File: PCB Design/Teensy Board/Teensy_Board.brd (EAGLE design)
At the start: 100 x 80 mm, 8 parts, among them IC1 MC7805BDTRKG, IC2 UA78M33CKVU, X1 RJ45-8X

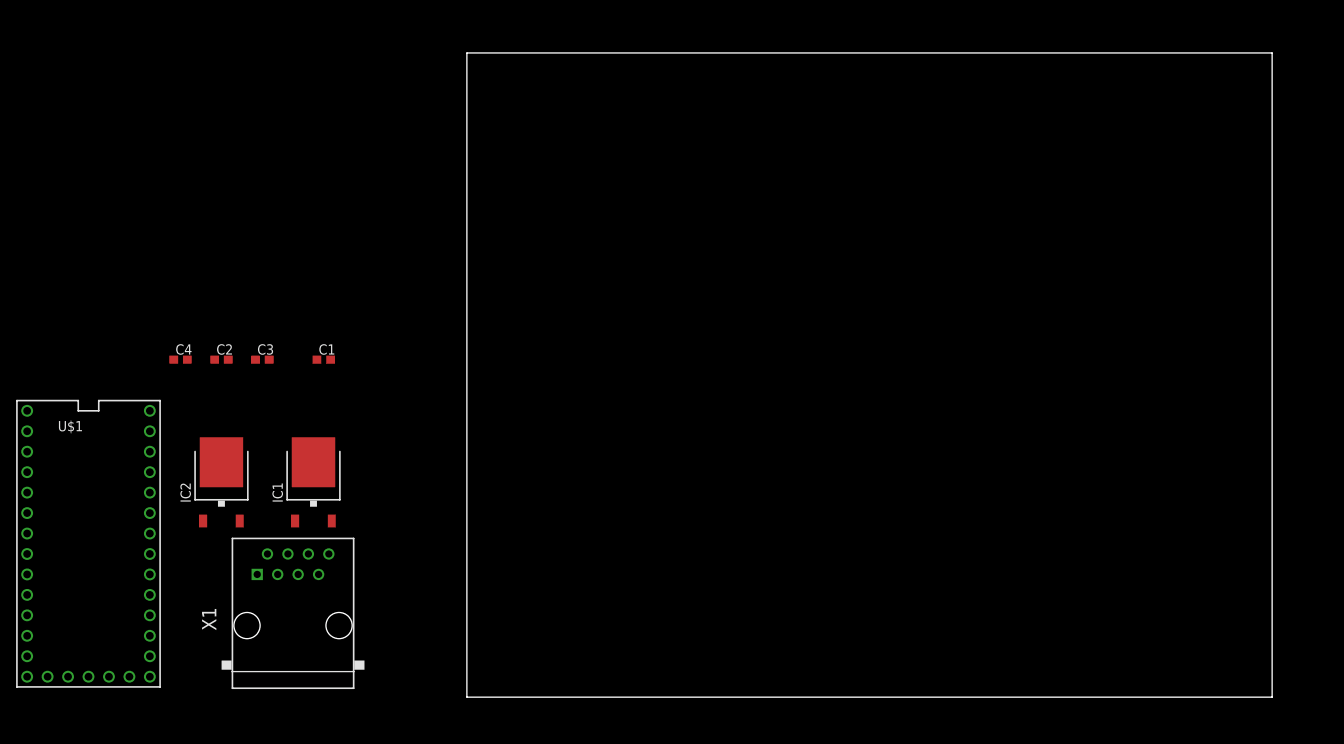
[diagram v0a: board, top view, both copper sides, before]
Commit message: Teensy Board change
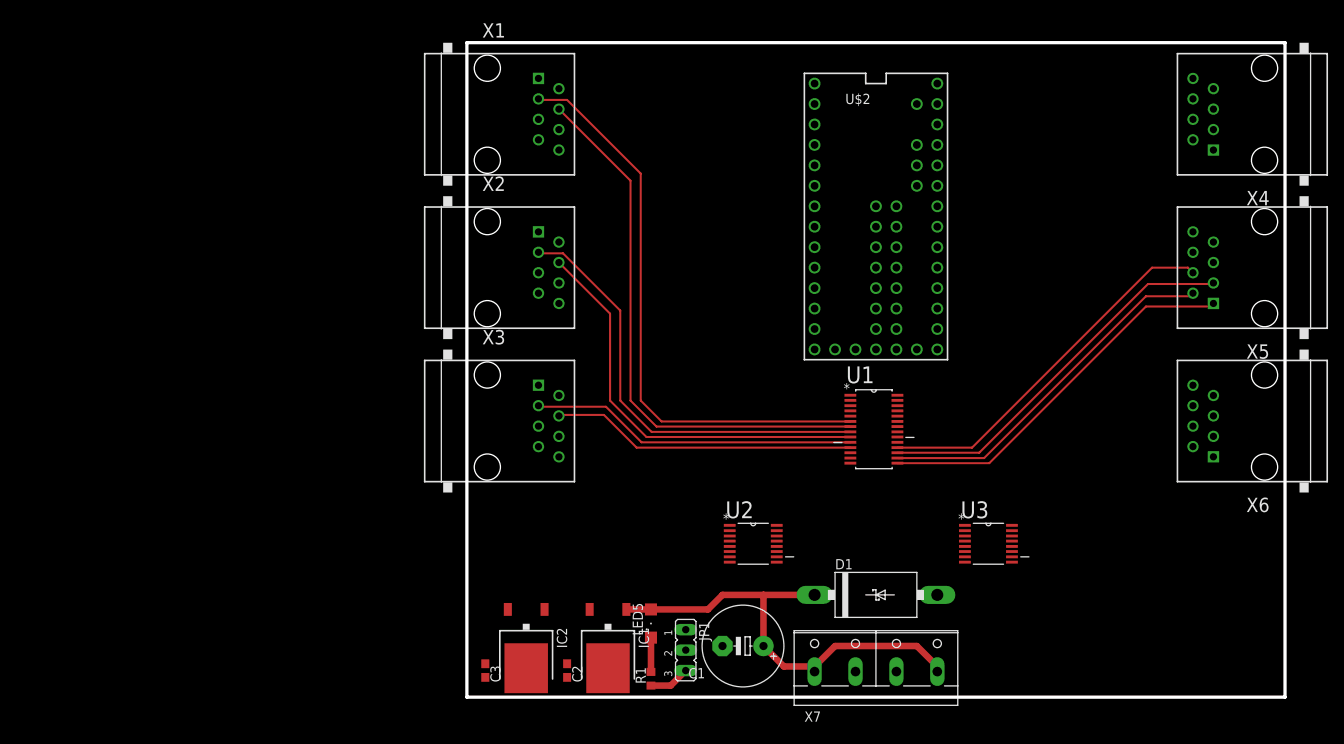
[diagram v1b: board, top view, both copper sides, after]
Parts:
- removed C4: 1uF, rcl:C0603
- removed U$1: TEENSY_3.1_BASIC, Teensy_3_Series_Board_v1.0:TEENSY_3.1_BASIC
- added D1: SB540E-G, CBLA_Test_bed_Library:DO201T15
- added JP1: (no value), jumper:JP2
- added LED5: (no value), led:SML1206
- added R1: 470, CBLA_Test_bed_Library:R0603
- added U$2: TEENSY_3.1_ALL_PINS_AND_PADS, Teensy_3_Series_Board_v1.0:TEENSY_3.1_ALLPINS
- added U1: PCA9685PW, NXP_By_element14_Batch_1:SOP65P640X110-28N
- added U2, U3: 74HC4051PW,118, NXP_By_element14_Batch_1:SOP65P640X110-16N
- added X2, X3, X4, X5, X6: RJ45-8X, CBLA_Test_bed_Library:RJ45-NO-SHIELD
- added X7: (no value), con-wago-508:W237-4P
- C1: device rcl:C0603 -> rcl:E5-10,5
- C3: value 470uF -> 1uF
- moved X1 67.9 mm to (2.54, 72.4), turned to 270 degrees
- moved C1 63.1 mm to (34.3, 6.35), turned to 180 degrees
- moved C2 57.7 mm to (12.4, 3.30), turned to 270 degrees
- moved C3 47.5 mm to (2.29, 3.30), turned to 270 degrees
- moved IC2 43.1 mm to (7.37, 6.10), turned to 180 degrees
- moved IC1 42.0 mm to (17.5, 6.10), turned to 180 degrees
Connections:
- new net AREF: U$2.AREF
- new net N$1: U1.6, X1.3
- new net N$10: LED5.C, R1.2
- new net N$11: U1.15, X5.1
- new net N$12: U1.16, X5.2
- new net N$13: U1.17, X5.3
- new net N$14: U1.18, X5.4
- new net N$15: U1.19, X6.1
- new net N$16: U1.20, X6.2
- new net N$17: U1.21, X6.3
- new net N$18: U1.22, X6.4
- new net N$2: U1.7, X1.4
- new net N$3: U1.8, X2.3
- new net N$4: U1.9, X2.4
- new net N$5: U1.10, X3.3
- new net N$6: U1.11, X3.4
- new net N$7: U1.12, X4.3
- new net N$8: U1.13, X4.4
- new net PWR_LED_GND: JP1.3, R1.1
- new net VCC: U2.16, U3.16
- new net VDD: U1.28
- new net VEE: U2.7, U3.7
- new net VUSB: U$2.VUSB
- net +12V: now also C1.+, D1.C, LED5.A, X7.1, X7.4; no longer C1.1, C3.1
- net +3V3: now also C3.1; no longer C4.1
- net 3.3V: now also U$2.3.3V, U$2.3.3V1, U$2.3.3V2; no longer U$1.3.3V, U$1.3.3V1
- net AGND: now also U$2.AGND; no longer U$1.AGND
- net GND: now also C1.-, D1.A, IC1.4, JP1.2, U$2.GND, U$2.GND1, U$2.GND2, U1.1, U1.14, U1.2, U1.23, U1.24, U1.25, U1.3, U1.4, U1.5, X7.2, X7.3; no longer C1.2, C4.2, U$1.GND, U$1.GND1
- net VBAT: now also U$2.VBAT; no longer U$1.VBAT
- net VIN: now also U$2.VIN; no longer U$1.VIN
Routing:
- net N$1: track 0.00 -> 71.8 mm
- net N$2: track 0.00 -> 68.5 mm
- net +12V: track 0.00 -> 56.5 mm
- net N$3: track 0.00 -> 54.5 mm
- net N$4: track 0.00 -> 51.5 mm
- net N$13: track 0.00 -> 48.0 mm
- net N$11: track 0.00 -> 47.5 mm
- net N$14: track 0.00 -> 46.2 mm
- net N$12: track 0.00 -> 45.2 mm
- net N$5: track 0.00 -> 40.6 mm
- net N$6: track 0.00 -> 37.9 mm
- net PWR_LED_GND: track 0.00 -> 5.09 mm
- net N$10: track 0.00 -> 4.26 mm
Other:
- board size 100 x 80 mm -> 101.6 x 81.3 mm

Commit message: Teensy Board Update
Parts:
- added C4, C5: 100nF, rcl:C0603
- added LED2, LED3: (no value), led:SML1206
- added R2, R3: 4k7, CBLA_Test_bed_Library:R0603
- added R4, R5: 470, CBLA_Test_bed_Library:R0603
- moved U2 5.08 mm to (40.6, 19.1)
- moved U3 5.08 mm to (59.7, 19.1)
- renumbered LED5 to LED1
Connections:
- removed net VDD: U1.28
- new net FPWM_1_1: U$2.3, X1.1
- new net FPWM_1_2: U$2.4, X1.2
- new net FPWM_2_1: U$2.5, X2.1
- new net FPWM_2_2: U$2.6, X2.2
- new net FPWM_3_1: U$2.22/A8, X3.1
- new net FPWM_3_2: U$2.23/A9, X3.2
- new net FPWM_4_1: U$2.25, X4.1
- new net FPWM_4_2: U$2.32, X4.2
- new net MUL_ADR_0: U$2.2, U2.11, U3.11
- new net MUL_ADR_1: U$2.24, U2.10, U3.10
- new net MUL_ADR_2: U$2.33, U2.9, U3.9
- new net MUL_SCL: U$2.19/A5, U3.3
- new net MUL_SCL_1: U3.13, X1.7
- new net MUL_SCL_2: U3.14, X2.7
- new net MUL_SCL_3: U3.15, X3.7
- new net MUL_SCL_4: U3.12, X4.7
- new net MUL_SCL_5: U3.1, X5.7
- new net MUL_SCL_6: U3.5, X6.7
- new net MUL_SDA: U$2.18/A4, U2.3
- new net MUL_SDA_1: U2.13, X1.8
- new net MUL_SDA_2: U2.14, X2.8
- new net MUL_SDA_3: U2.15, X3.8
- new net MUL_SDA_4: U2.12, X4.8
- new net MUL_SDA_5: U2.1, X5.8
- new net MUL_SDA_6: U2.5, X6.8
- new net N$19: LED3.C, R5.2
- new net N$31: X1.5
- new net N$32: X1.6
- new net N$33: U1.22
- new net N$35: X2.5
- new net N$36: X2.6
- new net N$39: X3.5
- new net N$40: X3.6
- new net N$43: X4.5
- new net N$44: X4.6
- new net N$47: X5.5
- new net N$48: X5.6
- new net N$51: X6.5
- new net N$52: X6.6
- new net SCL_PWM: R3.1, U$2.29, U1.26
- new net SDA_PWM: R2.1, U$2.30, U1.27
- net +3V3: now also C5.1, LED2.A, R2.2, R3.2, U1.28
- net +5V: now also C4.1, LED3.A
- net GND: now also C4.2, C5.2, R4.1, R5.1
- net N$18: now also LED2.C, R4.2; no longer U1.22, X6.4

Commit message: Teensy Board
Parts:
- added JP2, JP3: (no value), jumper:JP2
- added R6: 4k7, CBLA_Test_bed_Library:R0603
- added T1: (no value), CBLA_Test_bed_Library:DPACK
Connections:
- removed net 3.3V: U$2.3.3V, U$2.3.3V1, U$2.3.3V2
- removed net N$31: X1.5
- removed net N$32: X1.6
- removed net N$35: X2.5
- removed net N$36: X2.6
- removed net N$39: X3.5
- removed net N$40: X3.6
- removed net N$43: X4.5
- removed net N$44: X4.6
- removed net N$47: X5.5
- removed net N$48: X5.6
- removed net N$51: X6.5
- removed net N$52: X6.6
- removed net VCC: U2.16, U3.16
- removed net VEE: U2.7, U3.7
- removed net VIN: U$2.VIN
- new net 3V3INT: JP3.2, R2.2, R3.2, U1.28, U2.16, U3.16
- new net A0: U$2.14/A0, X1.5
- new net A1: U$2.15/A1, X1.6
- new net A12: U$2.A12, X3.5
- new net A13: U$2.A13, X3.6
- new net A15: U$2.26, X4.5
- new net A16: U$2.27, X5.5
- new net A17: U$2.28, X5.6
- new net A2: U$2.16/A2, X2.5
- new net A20: U$2.31, X4.6
- new net A3: U$2.17/A3, X2.6
- new net A6: U$2.20/A6, X6.5
- new net A7: U$2.21/A7, X6.6
- new net N$20: R6.2, T1.1
- new net PGM: T1.2, U$2.PGM
- new net TEENSY_3V3: JP3.3, U$2.3.3V, U$2.3.3V1, U$2.3.3V2
- new net TEENSY_VIN: JP2.2, U$2.VIN
- net +3V3: now also JP3.1; no longer R2.2, R3.2, U1.28
- net +5V: now also JP2.1
- net GND: now also R6.1, T1.3, U2.6, U2.7, U2.8, U3.6, U3.7, U3.8

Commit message: teensy PCB
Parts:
- removed JP1: (no value), jumper:JP2
- removed T1: (no value), CBLA_Test_bed_Library:DPACK
- added Q1: (no value), transistors:SOT-23
- added SV1: (no value), con-lstb:MA04-1
- added SV2: (no value), con-lstb:MA04-2
- added SV3, SV4, SV5, SV6, SV7, SV8: (no value), con-lstb:MA08-1
- moved LED2 167.3 mm to (-92.7, 105.4)
- moved R6 163.5 mm to (-81.3, 106.7)
- moved JP2 159.6 mm to (-82.5, 100.3)
- moved JP3 159.6 mm to (-91.4, 100.3)
- moved R5 158.8 mm to (-66.0, 106.7)
- moved LED3 158.1 mm to (-16.5, 111.8)
- moved R4 147.4 mm to (-61.0, 106.7)
- moved LED1 145.6 mm to (-86.4, 105.4), turned to 0 degrees
- moved R3 140.7 mm to (-76.2, 106.7)
- moved C5 135.9 mm to (-40.6, 106.7)
- moved R2 133.7 mm to (-71.1, 106.7)
- moved X7 132.9 mm to (-67.3, 64.8)
- moved C1 132.5 mm to (-74.9, 81.3), turned to 0 degrees
- moved R1 130.8 mm to (-55.9, 106.7), turned to 0 degrees
- moved C4 129.1 mm to (-33.0, 106.7)
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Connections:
- removed net A6: U$2.20/A6, X6.5
- removed net A7: U$2.21/A7, X6.6
- removed net FPWM_3_1: U$2.22/A8, X3.1
- removed net FPWM_3_2: U$2.23/A9, X3.2
- removed net N$1: U1.6, X1.3
- removed net N$11: U1.15, X5.1
- removed net N$12: U1.16, X5.2
- removed net N$13: U1.17, X5.3
- removed net N$14: U1.18, X5.4
- removed net N$15: U1.19, X6.1
- removed net N$16: U1.20, X6.2
- removed net N$17: U1.21, X6.3
- removed net N$2: U1.7, X1.4
- removed net N$20: R6.2, T1.1
- removed net N$3: U1.8, X2.3
- removed net N$33: U1.22
- removed net N$4: U1.9, X2.4
- removed net N$5: U1.10, X3.3
- removed net N$6: U1.11, X3.4
- removed net N$7: U1.12, X4.3
- removed net N$8: U1.13, X4.4
- removed net PWR_LED_GND: JP1.3, R1.1
- new net A8: SV6.5, U$2.22/A8, X4.5
- new net A9: SV6.6, U$2.23/A9, X4.6
- new net CE: SV2.3, U$2.9
- new net CSN: SV2.4, U$2.10
- new net FPWM_5_1: SV7.1, U$2.25, X5.1
- new net FPWM_5_2: SV7.2, U$2.32, X5.2
- new net MISO: SV2.7, U$2.12
- new net MOSI: SV2.6, U$2.11
- new net PGM_DO: Q1.1, R6.2, U$2.0
- new net SCK: SV2.5, U$2.13
- new net SPWM_1_1: SV3.3, U1.6, X1.3
- new net SPWM_1_2: SV3.4, U1.7, X1.4
- new net SPWM_2_1: SV4.3, U1.8, X2.3
- new net SPWM_2_2: SV4.4, U1.9, X2.4
- new net SPWM_3_1: SV5.1, U1.10, X3.1
- new net SPWM_3_2: SV5.2, U1.11, X3.2
- new net SPWM_3_3: SV5.3, U1.12, X3.3
- new net SPWM_3_4: SV5.4, U1.13, X3.4
- new net SPWM_4_1: SV6.3, U1.21, X4.3
- new net SPWM_4_2: SV6.4, U1.22, X4.4
- new net SPWM_5_1: SV7.3, U1.19, X5.3
- new net SPWM_5_2: SV7.4, U1.20, X5.4
- new net SPWM_6_1: SV8.1, U1.15, X6.1
- new net SPWM_6_2: SV8.2, U1.16, X6.2
- new net SPWM_6_3: SV8.3, U1.17, X6.3
- new net SPWM_6_4: SV8.4, U1.18, X6.4
- net 3V3INT: now also SV1.4, SV2.2
- net A0: now also SV8.5, X6.5; no longer X1.5
- net A1: now also SV8.6, X6.6; no longer X1.6
- net A12: now also SV4.5, X2.5; no longer X3.5
- net A13: now also SV3.5, X1.5; no longer X3.6
- net A15: now also SV4.6, X2.6; no longer X4.5
- net A16: now also SV5.5, X3.5; no longer X5.5
- net A17: now also SV5.6, X3.6; no longer X5.6
- net A2: now also SV7.5, X5.5; no longer X2.5
- net A20: now also SV3.6, X1.6; no longer X4.6
- net A3: now also SV7.6, X5.6; no longer X2.6
- net FPWM_1_1: now also SV3.1
- net FPWM_1_2: now also SV3.2
- net FPWM_2_1: now also SV4.1
- net FPWM_2_2: now also SV4.2
- net FPWM_4_1: now also SV6.1, U$2.20/A6; no longer U$2.25
- net FPWM_4_2: now also SV6.2, U$2.21/A7; no longer U$2.32
- net GND: now also Q1.2, R1.1, SV1.1, SV2.1; no longer JP1.2, T1.3
- net MUL_SCL_1: now also SV3.7, U3.1; no longer U3.13
- net MUL_SCL_2: now also SV4.7, U3.2; no longer U3.14
- net MUL_SCL_3: now also SV5.7, U3.4; no longer U3.15
- net MUL_SCL_4: now also SV6.7, U3.15; no longer U3.12
- net MUL_SCL_5: now also SV7.7, U3.14; no longer U3.1
- net MUL_SCL_6: now also SV8.7, U3.13; no longer U3.5
- net MUL_SDA_1: now also SV3.8, U2.1; no longer U2.13
- net MUL_SDA_2: now also SV4.8, U2.2; no longer U2.14
- net MUL_SDA_3: now also SV5.8, U2.4; no longer U2.15
- net MUL_SDA_4: now also SV6.8, U2.15; no longer U2.12
- net MUL_SDA_5: now also SV7.8, U2.14; no longer U2.1
- net MUL_SDA_6: now also SV8.8, U2.13; no longer U2.5
- net PGM: now also Q1.3; no longer T1.2
- net SCL_PWM: now also SV1.2
- net SDA_PWM: now also SV1.3
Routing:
- net MUL_SCL_4: track 0.00 -> 73.7 mm
- net N$1: track 71.8 -> 0.00 mm
- net N$2: track 68.5 -> 0.00 mm
- net MUL_SDA_4: track 0.00 -> 67.0 mm
- net SPWM_1_1: track 0.00 -> 66.3 mm
- net SPWM_4_2: track 0.00 -> 65.5 mm
- net SPWM_1_2: track 0.00 -> 65.5 mm
- net SPWM_4_1: track 0.00 -> 64.0 mm
- net MUL_SCL_5: track 0.00 -> 62.1 mm, vias 0 -> 1
- net +12V: track 56.5 -> 0.00 mm
- net N$3: track 54.5 -> 0.00 mm
- net N$4: track 51.5 -> 0.00 mm
- net A1: track 0.00 -> 50.5 mm
- net A0: track 0.00 -> 50.5 mm
- net N$13: track 48.0 -> 0.00 mm
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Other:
- board size 101.6 x 81.3 mm -> 100 x 80 mm

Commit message: Teensy Board
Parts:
- moved LED1 176.2 mm to (60.7, 8.38), turned to 90 degrees
- moved JP3 174.5 mm to (61.0, 15.2)
- moved C1 164.1 mm to (71.1, 6.35), turned to 90 degrees
- moved R3 158.4 mm to (55.4, 18.5)
- moved R1 155.5 mm to (60.7, 3.81), turned to 90 degrees
- moved JP2 145.6 mm to (35.6, 15.2)
- moved R2 142.7 mm to (41.1, 18.5), turned to 180 degrees
- moved D1 139.5 mm to (87.6, 6.35)
- moved LED2 135.8 mm to (2.29, 8.38), turned to 90 degrees
- moved R4 131.7 mm to (21.3, 3.81), turned to 90 degrees
- moved X7 130.1 mm to (48.3, 5.08)
- moved R6 128.1 mm to (36.6, 56.4)
- moved C3 127.7 mm to (24.9, 3.81), turned to 270 degrees
- moved R5 123.5 mm to (2.29, 3.81), turned to 90 degrees
- moved SV2 119.5 mm to (33.0, 74.9)
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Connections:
- removed net A20: SV3.6, U$2.31, X1.6
- new net A11: SV3.5, U$2.A11, X1.5
- net +3V3: now also LED3.A; no longer LED2.A
- net +5V: now also LED2.A; no longer LED3.A
- net A13: now also SV3.6, X1.6; no longer SV3.5, X1.5
- net FPWM_2_1: now also U$2.6; no longer U$2.5
- net FPWM_2_2: now also U$2.5; no longer U$2.6
- net N$18: now also LED3.C; no longer LED2.C
- net N$19: now also LED2.C; no longer LED3.C
- net PGM_DO: now also U$2.7; no longer U$2.0
- net SCL_PWM: now also SV1.3; no longer SV1.2
- net SDA_PWM: now also SV1.2; no longer SV1.3
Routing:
- net TEENSY_VIN: track 0.00 -> 166.1 mm, vias 0 -> 1
- net 3V3INT: track 0.00 -> 152.9 mm, vias 0 -> 3
- net TEENSY_3V3: track 0.00 -> 138.5 mm
- net A12: track 0.00 -> 106.6 mm
- net A11: track 0.00 -> 86.5 mm
- net A13: track 0.00 -> 82.0 mm
- net FPWM_2_2: track 0.00 -> 79.2 mm
- net +12V: track 0.00 -> 74.8 mm
- net FPWM_2_1: track 0.00 -> 74.8 mm
- net MUL_ADR_1: track 0.00 -> 68.2 mm, vias 0 -> 4
- net MUL_ADR_0: track 0.00 -> 65.4 mm, vias 0 -> 3
- net PGM: track 0.00 -> 57.6 mm, vias 0 -> 1
- net SCK: track 0.00 -> 55.4 mm, vias 0 -> 2
- net SCL_PWM: track 0.00 -> 48.5 mm, vias 0 -> 1
- net +3V3: track 0.00 -> 47.9 mm
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- added copper zone on layer 1, net GND
- added copper zone on layer 16, net GND
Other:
- board size 100 x 80 mm -> 98.7 x 81.3 mm
- board text added: "+12"
- board text added: "GND"
- board text added: "Teesny Board"

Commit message: Teensy Board
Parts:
- added X8: UART, CBLA_Test_bed_Library:1X02
- Q1: value (none) -> PROGRAM_FET
- SV1: value (none) -> PWM_I2C
- SV2: value (none) -> SPI
- moved SV2 3.30 mm to (30.0, 76.2)
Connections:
- new net RX1: U$2.0, X8.2
- new net TX1: U$2.1, X8.1
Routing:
- net MUL_ADR_0: track 65.4 -> 101.5 mm, vias 3 -> 5
- net TX1: track 0.00 -> 4.35 mm
- net RX1: track 0.00 -> 4.35 mm
- net SCK: track 55.4 -> 59.8 mm
- net 3V3INT: track 152.9 -> 157.2 mm
- net MUL_ADR_2: track 29.5 -> 33.7 mm
- net MISO: track 43.4 -> 47.2 mm
- net CE: track 31.8 -> 35.7 mm
- net MOSI: track 37.2 -> 40.2 mm
- net CSN: track 45.6 -> 48.1 mm
- net GND: vias 4 -> 17
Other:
- board text added: "08/14"
- board text added: "MOSI"
- board text added: "SPI"
- board text added: "UART"

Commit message: Teensy
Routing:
- net SCL_PWM: track 48.5 -> 50.3 mm
- net MUL_SCL_2: track 39.3 -> 40.8 mm
- net SDA_PWM: track 47.4 -> 48.4 mm
- net 3V3INT: track 157.2 -> 158.1 mm
- net MUL_ADR_2: track 33.7 -> 33.0 mm
- net GND: vias 17 -> 19
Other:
- board text added: "+3.3V"
- board text added: "ANLG_1"
- board text added: "ANLG_2"
- board text added: "CE"
- board text added: "CSN"
- board text added: "FPWM_1"
- board text added: "FPWM_2"
- board text added: "INT"
- board text added: "MISO"
- board text added: "PWM I2C"
- board text added: "REG"
- board text added: "RX"
- board text added: "SCK"
- board text added: "SCL"
- board text added: "SDA"
- board text added: "SPWM_1"
- board text added: "SPWM_2"
- board text added: "SPWM_3"
- board text added: "SPWM_4"
- board text added: "TEENSY"
- board text added: "TEENSY PWR"
- board text added: "TX"
- board text added: "USB\"
